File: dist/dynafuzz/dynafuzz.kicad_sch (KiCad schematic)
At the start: 56 parts, among them J1 AudioJack_IN, J2 AudioJack_OUT, J3 Jack-DC, J4 MAIN_BIC, J5 SWITCH_BIC, Q1 Q_NPN, Q2 Q_NPN, Q3 Q_NPN, Q4 Q_NPN, SW1 SW_3PDT_x3

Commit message: rev B - dynafuzz
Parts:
- added TP1, TP2, TP3, TP4, TP5: ~, TestPoint:TestPoint_Pad_D1.5mm, symbol Connector:TestPoint
- R18: value 1K -> 3.3k
- R23: value 100 -> 3.3k
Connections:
- net at C10.2, C9.2, D3.2 (A)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: now also TP3.1
- net at C12.2, RV3.2: now also TP4.1
- net at C2.2, C3.1, Q1.3 (C)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: now also TP1.1
- net at C13.1, Q4.3 (C), R22.2: now also TP5.1
- net at C6.2, C7.1, D1.2 (A)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: now also TP2.1

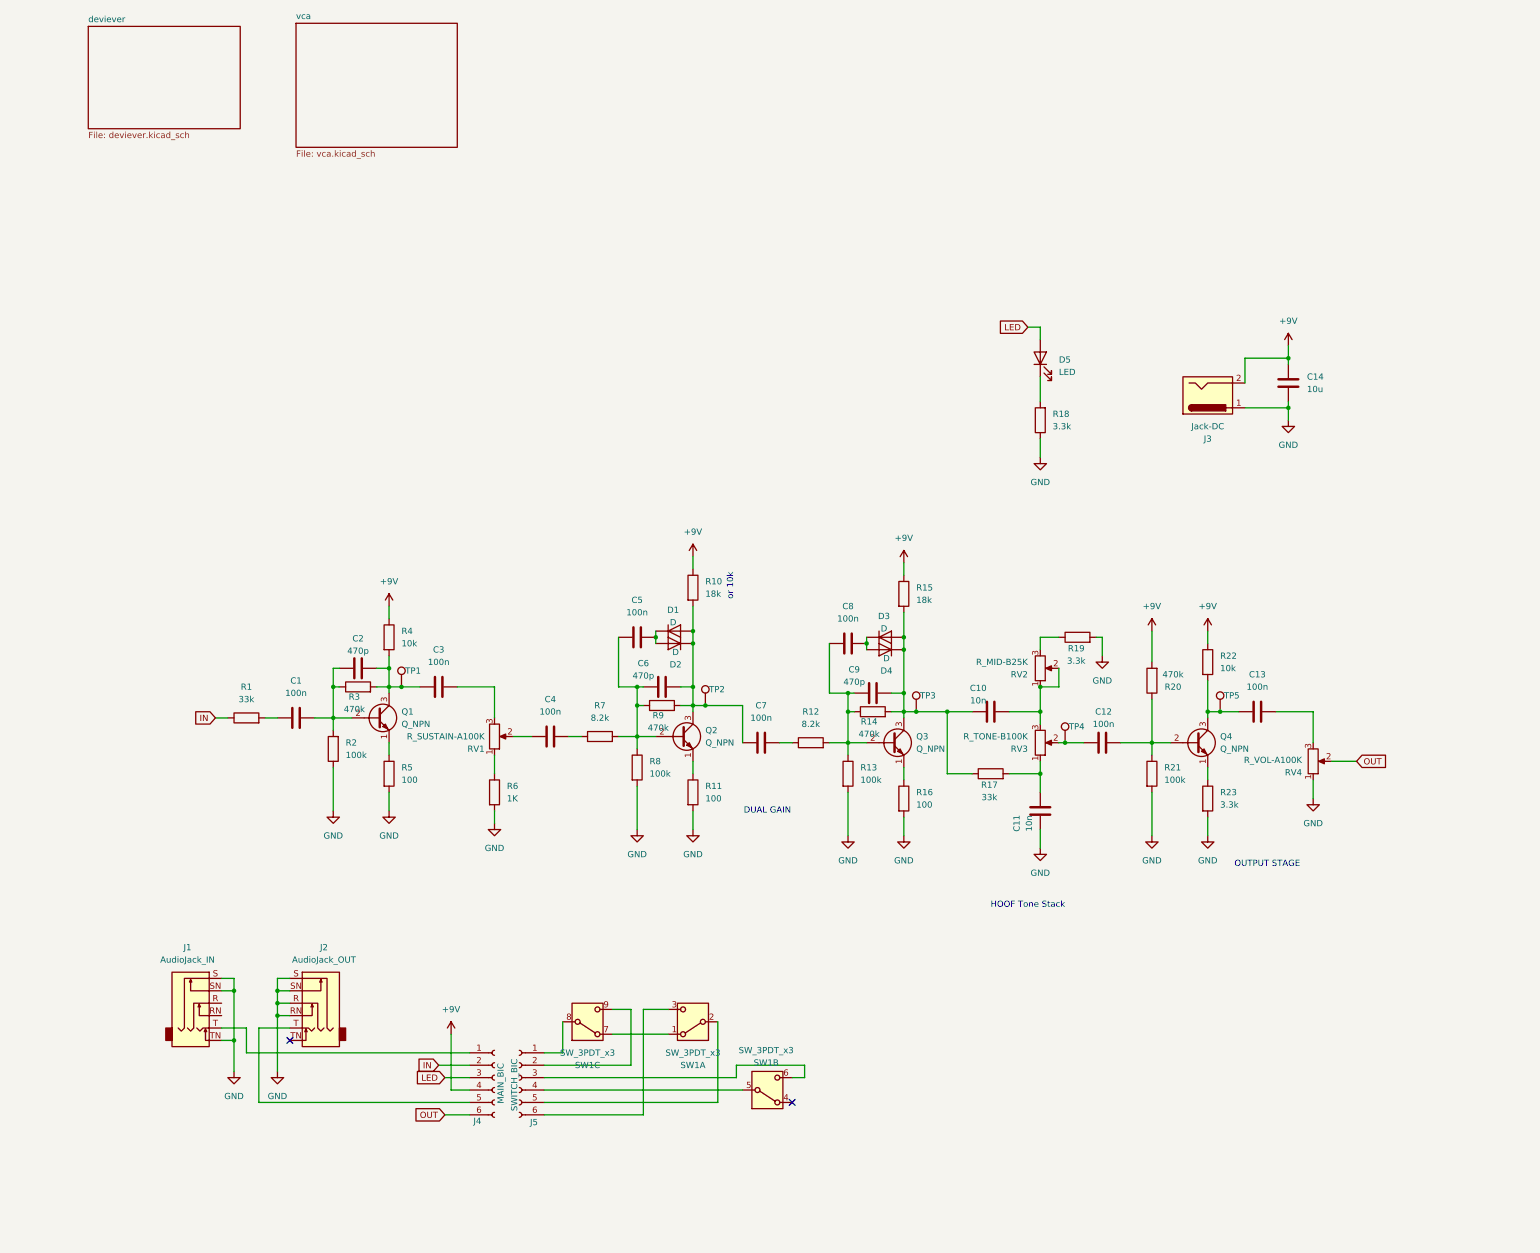
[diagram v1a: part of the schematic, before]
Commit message: add vca envelope detector to dynafuzz
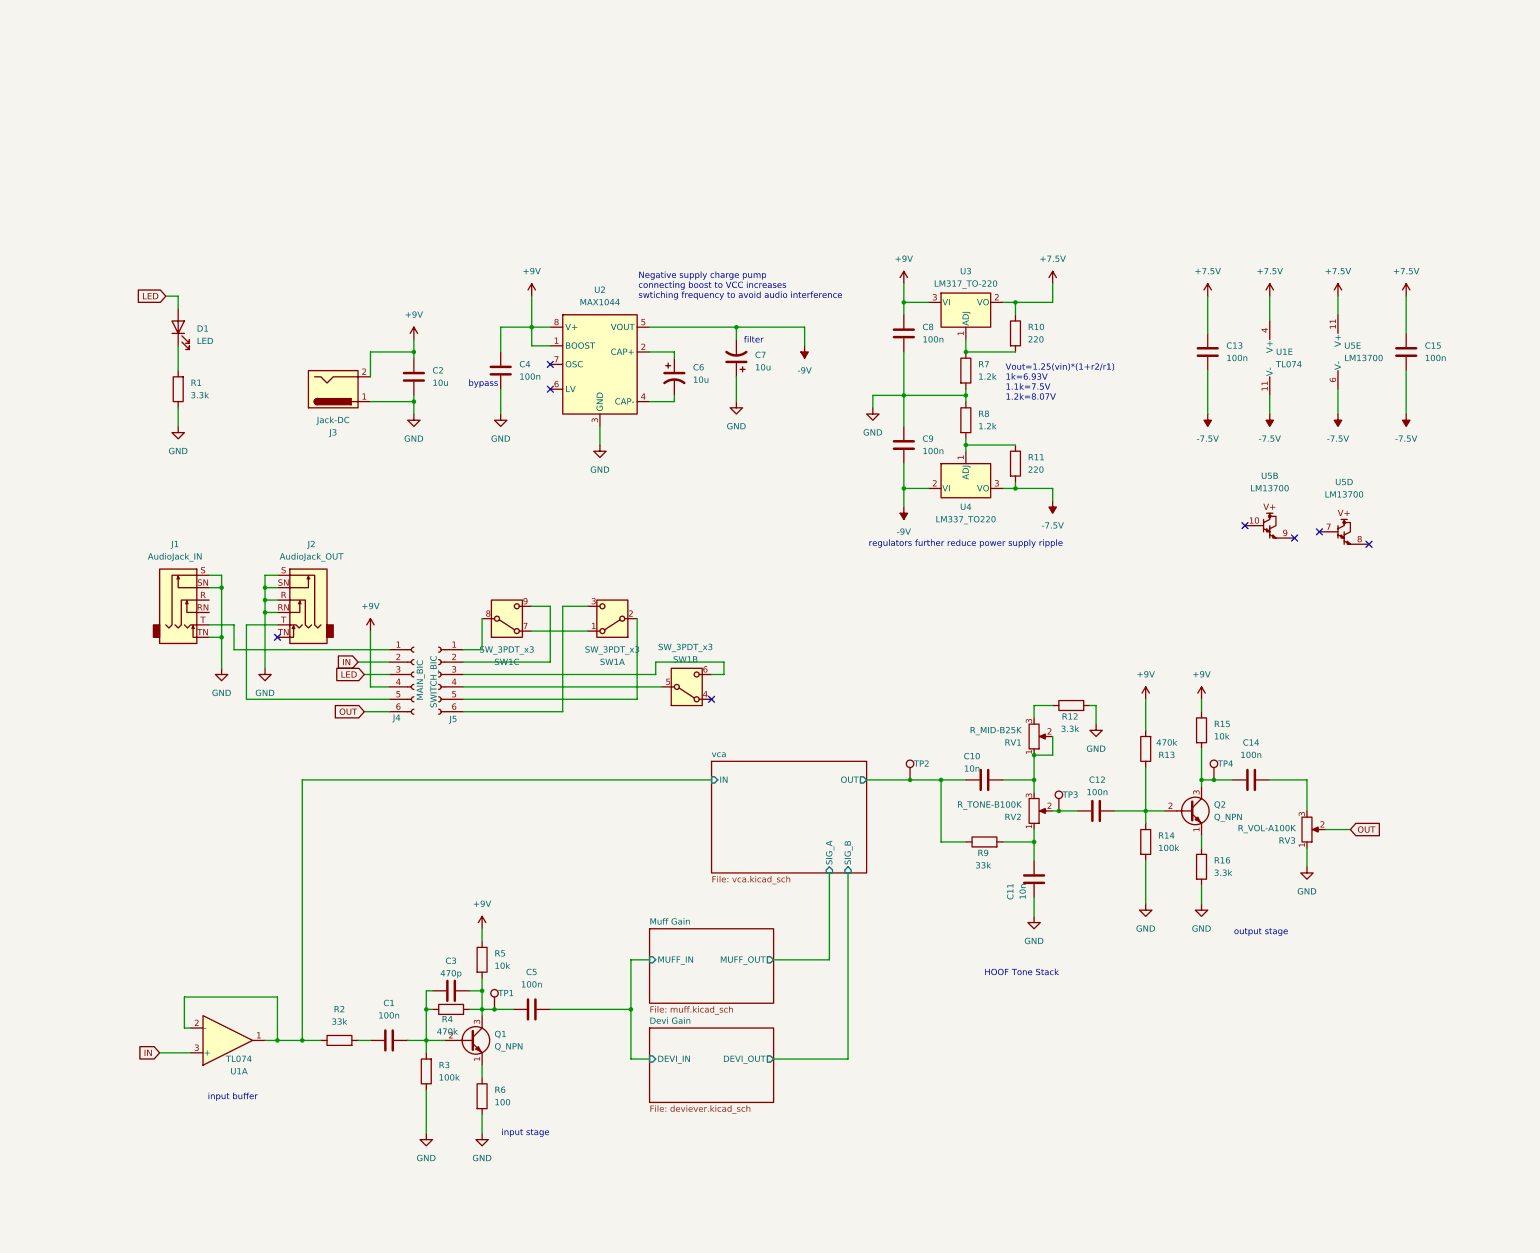
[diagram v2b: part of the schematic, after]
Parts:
- removed C5, C7: 100n, _project:C, symbol Device:C
- removed C6: 470p, _project:C, symbol Device:C
- removed D1, D2, D3, D4: D, Diode_THT:D_A-405_P2.54mm_Vertical_KathodeUp, symbol Device:D
- removed Q2, Q3: Q_NPN, Package_TO_SOT_THT:TO-92_Inline, symbol Transistor_BJT:2N3904
- removed R12: 8.2k, _project:R, symbol Device:R
- removed R13: 100k, _project:R, symbol Device:R
- removed R14, R9: 470k, _project:R, symbol Device:R
- removed R15: 18k, _project:R, symbol Device:R
- removed R16: 100, _project:R, symbol Device:R
- removed R6: 1K, _project:R, symbol Device:R
- removed RV1: R_SUSTAIN-A100K, _effects_shared_footprints:Potentiometer_Alpha_RD901F-40-00D_Single_Vertical, symbol Device:R_Potentiometer
- removed TP2: ~, TestPoint:TestPoint_Pad_D1.5mm, symbol Connector:TestPoint
- added C13, C15: 100n, Capacitor_SMD:C_0805_2012Metric, symbol Device:C
- added C6, C7: 10u, Capacitor_SMD:CP_Elec_5x3, symbol Device:C_Polarized_US
- added U1: TL074, Package_SO:SSOP-14_5.3x6.2mm_P0.65mm, symbol Amplifier_Operational:TL074
- added U2: MAX1044, Package_DIP:DIP-8_W7.62mm, symbol Regulator_SwitchedCapacitor:MAX1044
- added U3: LM317_TO-220, Package_TO_SOT_THT:TO-220-3_Vertical, symbol Regulator_Linear:LM317_TO-220
- added U4: LM337_TO220, Package_TO_SOT_THT:TO-220-3_Vertical, symbol Regulator_Linear:LM337_TO220
- added U5: LM13700, Package_SO:SOIC-16_3.9x9.9mm_P1.27mm, symbol Amplifier_Operational:LM13700
- C1, C10, C11, C12, C4, C8: footprint _project:C -> Capacitor_SMD:C_0805_2012Metric
- C14: renamed from C13; footprint _project:C -> Capacitor_SMD:C_0805_2012Metric
- C2: renamed from C14; footprint Capacitor_THT:CP_Radial_D6.3mm_P2.50mm -> Capacitor_SMD:CP_Elec_5x3
- C3: renamed from C2; footprint _project:C -> Capacitor_SMD:C_0805_2012Metric
- C5: renamed from C3; footprint _project:C -> Capacitor_SMD:C_0805_2012Metric
- C9: value 470p -> 100n; footprint _project:C -> Capacitor_SMD:C_0805_2012Metric
- R1: renamed from R18; footprint _project:R -> Resistor_SMD:R_0805_2012Metric
- R10: value 18k -> 220; footprint _project:R -> Resistor_SMD:R_0805_2012Metric
- R11: value 100 -> 220; footprint _project:R -> Resistor_SMD:R_0805_2012Metric
- R12: renamed from R19; footprint _project:R -> Resistor_SMD:R_0805_2012Metric
- R13: renamed from R20; footprint _project:R -> Resistor_SMD:R_0805_2012Metric
- R14: renamed from R21; footprint _project:R -> Resistor_SMD:R_0805_2012Metric
- R15: renamed from R22; footprint _project:R -> Resistor_SMD:R_0805_2012Metric
- R16: renamed from R23; footprint _project:R -> Resistor_SMD:R_0805_2012Metric
- R2: renamed from R1; footprint _project:R -> Resistor_SMD:R_0805_2012Metric
- R3: renamed from R2; footprint _project:R -> Resistor_SMD:R_0805_2012Metric
- R4: renamed from R3; footprint _project:R -> Resistor_SMD:R_0805_2012Metric
- R5: renamed from R4; footprint _project:R -> Resistor_SMD:R_0805_2012Metric
- R6: renamed from R5; footprint _project:R -> Resistor_SMD:R_0805_2012Metric
- R7: value 8.2k -> 1.2k; footprint _project:R -> Resistor_SMD:R_0805_2012Metric
- R8: value 100k -> 1.2k; footprint _project:R -> Resistor_SMD:R_0805_2012Metric
- R9: renamed from R17; footprint _project:R -> Resistor_SMD:R_0805_2012Metric
- renumbered D5 to D1, Q4 to Q2, RV2 to RV1, RV3 to RV2, RV4 to RV3, TP3 to TP2, TP4 to TP3, TP5 to TP4
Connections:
- net +9V: now also C4.1, C8.1, U2.1 (BOOST), U2.8 (V+), U3.3 (VI); no longer R10.1
- net GND: now also C4.2, C8.2, C9.1, R7.2, R8.1, C7.1, U2.3 (GND); no longer R11.2, R8.2
- net IN: now also U1.3 (+); no longer R2.1
- net Devi Gain/DEVI_IN: now reaches C5.2
- net vca/OUT: now reaches C10.2, R9.1, TP2.1
- net vca/OUT: no longer C9.2
- net at R10.2: now also R7.1, U3.1 (ADJ)
- net at R11.1: now also R8.2, U4.1 (ADJ)
- new net: C6.1, U2.2 (CAP+)
- new net: C6.2, U2.4 (CAP-)
- new net +7.5V: C13.1, C15.1, R10.1, U1.4 (V+), U3.2 (VO), U5.11 (V+)
- new net -7.5V: C13.2, C15.2, R11.2, U1.11 (V-), U4.3 (VO), U5.6 (V-)
- new net -9V: C7.2, C9.2, U2.5 (VOUT), U4.2 (VI)
- new net vca/IN: R2.1, U1.1, U1.2 (-)
- no-connect marks 2 -> 8
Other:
- sheet deviever renamed Devi Gain
- added sheet Muff Gain (muff.kicad_sch)
- sheet Devi Gain ports: added DEVI_IN, DEVI_OUT; removed none
- sheet vca ports: added IN, OUT, SIG_A, SIG_B; removed none
- note added: "Negative supply charge pump connecting boost to VCC increases swtiching frequency to avoid audio interference"
- note added: "Vout=1.25(vin)*(1+r2/r1) 1k=6.93V 1.1k=7.5V 1.2k=8.07V"
- note added: "bypass"
- note added: "filter"
- note added: "input buffer"
- note added: "input stage"
- note added: "output stage"
- note added: "regulators further reduce power supply ripple"
- note removed: "DUAL GAIN"
- note removed: "OUTPUT STAGE"
- note removed: "or 10k"
- moved on the sheet: C1, C10, C11, C12, C14, C2, C3, C5, D1, J1, J2, J3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

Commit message: start layout
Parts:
- U1: footprint Package_SO:SSOP-14_5.3x6.2mm_P0.65mm -> Package_SO:SOIC-14_3.9x8.7mm_P1.27mm
- U2: footprint Package_DIP:DIP-8_W7.62mm -> Package_SO:SOIC-8_3.9x4.9mm_P1.27mm
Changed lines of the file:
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@@
 			)
 		)
-		(property "Footprint" "Package_SO:SSOP-14_5.3x6.2mm_P0.65mm"
+		(property "Footprint" "Package_SO:SOIC-14_3.9x8.7mm_P1.27mm"
 			(at 33.02 173.99 0)
 			(effects
@@
 			)
 		)
-		(property "Footprint" "Package_DIP:DIP-8_W7.62mm"
+		(property "Footprint" "Package_SO:SOIC-8_3.9x4.9mm_P1.27mm"
 			(at 113.03 35.56 0)
 			(effects
@@
 			)
 		)
-		(property "Footprint" "Package_SO:SSOP-14_5.3x6.2mm_P0.65mm"
+		(property "Footprint" "Package_SO:SOIC-14_3.9x8.7mm_P1.27mm"
 			(at 248.92 29.21 0)
 			(effects

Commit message: updates
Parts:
- removed C13, C15: 100n, Capacitor_SMD:C_0805_2012Metric, symbol Device:C
- removed U1: TL074, Package_SO:SOIC-14_3.9x8.7mm_P1.27mm, symbol Amplifier_Operational:TL074
- removed U5: LM13700, Package_SO:SOIC-16_3.9x9.9mm_P1.27mm, symbol Amplifier_Operational:LM13700
- R13: renamed from R7; value 1.2k -> 1.1k
- R14: renamed from R8; value 1.2k -> 1.1k
- renumbered C12 to C10, C8 to C11, C9 to C12, C14 to C13, C3 to C2, C5 to C3, C2 to C4, C4 to C5, C10 to C6, C6 to C7, C11 to C8, C7 to C9, J4 to J3, J5 to J4, J3 to J5, R14 to R10, R15 to R11, R16 to R12, R10 to R15, R11 to R16, R9 to R7, R12 to R8, R13 to R9, U2 to U1, U3 to U2, U4 to U3
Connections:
- net vca/IN is gone; now on net IN: R2.1
- no-connect marks 8 -> 4
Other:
- sheet vca ports: added TRIGGER; removed IN
- note added: "NOTE: power supply is always active even when signal bypassed"
- note added: "TODO: switch to capacitor multiplier?"
- note added: "Vout=1.25V*(1+(r2/r1)) 1k=6.93V 1.1k=7.5V 1.2k=8.07V"
- note added: "envelope mixer"
- note added: "parallel gain stage"
- note added: "switch daughterboard"
- note removed: "Vout=1.25(vin)*(1+r2/r1) 1k=6.93V 1.1k=7.5V 1.2k=8.07V"
- note removed: "input buffer"
- moved on the sheet: C1, C11, C12, C2, C3, C4, C5, C7, C9, D1, J1, J2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

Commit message: update dynafuzz
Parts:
- R8: value 3.3k -> 1k
- RV1: value R_MID-B25K -> R_MID-B100K
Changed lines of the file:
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@@
 			)
 		)
-		(property "Value" "3.3k"
+		(property "Value" "1k"
 			(at 206.756 107.696 90)
 			(effects
@@
 			)
 		)
-		(property "Value" "R_MID-B25K"
+		(property "Value" "R_MID-B100K"
 			(at 196.85 107.9501 0)
 			(effects
